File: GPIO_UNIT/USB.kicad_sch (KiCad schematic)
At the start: 11 parts, among them J701 USB_B_Mini, U701 CH340G, Y701 Crystal

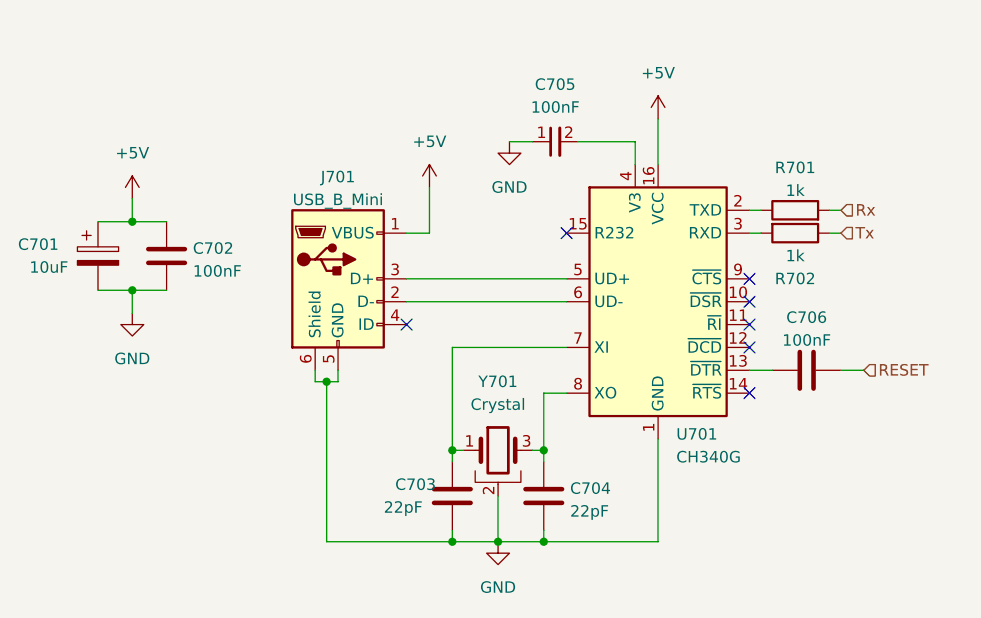
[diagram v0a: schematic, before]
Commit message: Digital pins are now able to use the analog pinnumbering as well. Pin can be set to an analog or digital pin number by simply pressing a or d respectively when editting the pinnumbers. Take note that one can fill in invalid analog pinnumbers. Also due to me support the arduino mega, I should remove pin number limit all togather.
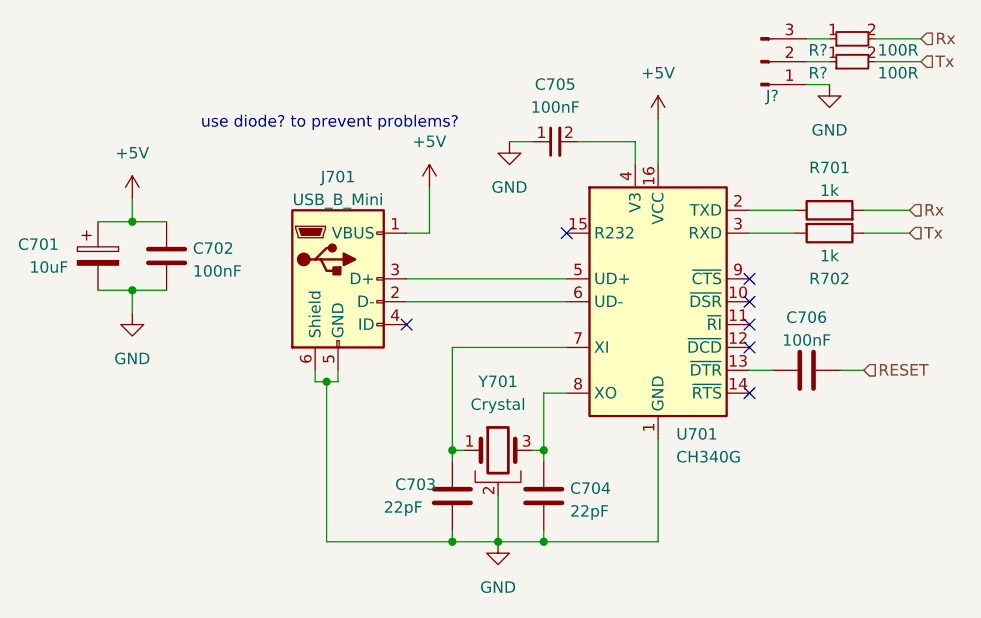
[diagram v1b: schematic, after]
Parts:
- added J?: Conn_01x03_Pin, symbol Connector:Conn_01x03_Pin
- added R? (x2): 100R, custom_kicad_lib_sk:R_0603_smalltext, symbol resistors_0603:R_100R_0603
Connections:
- net GND: now also J?.1 (Pin_1)
- net Rx: now also R?.2
- net Tx: now also R?.2
- new net: J?.3 (Pin_3), R?.1
- new net: J?.2 (Pin_2), R?.1
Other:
- note added: "use diode? to prevent problems?"
- moved on the sheet: R701, R702
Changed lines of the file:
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@@
     (stroke (width 0) (type default))
   )
-  (wire (pts (xy 134.62 83.82) (xy 133.35 83.82))
+  (wire (pts (xy 138.43 83.82) (xy 133.35 83.82))
     (stroke (width 0) (type default))
   )
@@
     (stroke (width 0) (type default))
   )
+  (wire (pts (xy 152.4 62.23) (xy 147.32 62.23))
+    (stroke (width 0) (type default))
+  )
   (wire (pts (xy 86.36 100.33) (xy 86.36 118.11))
     (stroke (width 0) (type default))
@@
     (stroke (width 0) (type default))
   )
-  (wire (pts (xy 143.51 83.82) (xy 142.24 83.82))
+  (wire (pts (xy 151.13 83.82) (xy 146.05 83.82))
     (stroke (width 0) (type default))
   )
@@
     (stroke (width 0) (type default))
   )
+  (wire (pts (xy 139.7 67.31) (xy 142.24 67.31))
+    (stroke (width 0) (type default))
+  )
   (wire (pts (xy 86.36 118.11) (xy 100.33 118.11))
     (stroke (width 0) (type default))
@@
     (stroke (width 0) (type default))
   )
+  (wire (pts (xy 139.7 64.77) (xy 142.24 64.77))
+    (stroke (width 0) (type default))
+  )
+  (wire (pts (xy 152.4 64.77) (xy 147.32 64.77))
+    (stroke (width 0) (type default))
+  )
   (wire (pts (xy 95.25 88.9) (xy 113.03 88.9))
     (stroke (width 0) (type default))
@@
     (stroke (width 0) (type default))
   )
+  (wire (pts (xy 139.7 62.23) (xy 142.24 62.23))
+    (stroke (width 0) (type default))
+  )
   (wire (pts (xy 113.03 96.52) (xy 100.33 96.52))
     (stroke (width 0) (type default))
@@
     (stroke (width 0) (type default))
   )
-  (wire (pts (xy 134.62 81.28) (xy 133.35 81.28))
+  (wire (pts (xy 138.43 81.28) (xy 133.35 81.28))
     (stroke (width 0) (type default))
   )
@@
     (stroke (width 0) (type default))
   )
-  (wire (pts (xy 143.51 81.28) (xy 142.24 81.28))
+  (wire (pts (xy 151.13 81.28) (xy 146.05 81.28))
     (stroke (width 0) (type default))
   )
@@
     (stroke (width 0) (type default))
   )
-  (hierarchical_label "Rx" (shape input) (at 143.51 81.28 0) (fields_autoplaced)
+  (text "use diode? to prevent problems?" (at 72.39 72.39 0)
+    (effects (font (size 1.27 1.27)) (justify left bottom))
+  )
+  (hierarchical_label "Tx" (shape input) (at 152.4 64.77 0) (fields_autoplaced)
     (effects (font (size 1.27 1.27)) (justify left))
   )
-  (hierarchical_label "Tx" (shape input) (at 143.51 83.82 0) (fields_autoplaced)
+  (hierarchical_label "Rx" (shape input) (at 152.4 62.23 0) (fields_autoplaced)
+    (effects (font (size 1.27 1.27)) (justify left))
+  )
+  (hierarchical_label "Rx" (shape input) (at 151.13 81.28 0) (fields_autoplaced)
+    (effects (font (size 1.27 1.27)) (justify left))
+  )
+  (hierarchical_label "Tx" (shape input) (at 151.13 83.82 0) (fields_autoplaced)
     (effects (font (size 1.27 1.27)) (justify left))
   )
@@
     )
   )
+  (symbol (lib_id "resistors_0603:R_100R_0603") (at 144.78 62.23 90) (unit 1)
+    (in_bom yes) (on_board yes) (dnp no)
+    (property "Reference" "R?" (at 140.97 63.5 90)
+      (effects (font (size 1.27 1.27)))
+    )
+    (property "Value" "100R" (at 149.86 63.5 90)
+      (effects (font (size 1.27 1.27)))
+    )
+    (property "Footprint" "custom_kicad_lib_sk:R_0603_smalltext" (at 142.24 59.69 0)
+      (effects (font (size 1.27 1.27)) hide)
+    )
+    (property "Datasheet" "" (at 144.78 64.77 0)
+      (effects (font (size 1.27 1.27)) hide)
+    )
+    (property "JLCPCB Part#" "C22775" (at 144.78 62.23 0)
+      (effects (font (size 1.27 1.27)) hide)
+    )
+    (pin "1")
+    (pin "2")
+    (instances
+      (project "GPIO_UNIT"
+        (path "/4337ba29-1ab5-4e01-8f76-ba2df9f917ea/a906ae47-0b9b-4d87-b0df-13938bf2addd"
+          (reference "R?") (unit 1)
+        )
+      )
+    )
+  )
   (symbol (lib_id "power:GND") (at 105.41 118.11 0) (unit 1)
     (in_bom yes) (on_board yes) (dnp no) (fields_autoplaced)
@@
     )
   )
-  (symbol (lib_id "Device:R") (at 138.43 83.82 270) (unit 1)
+  (symbol (lib_id "Device:R") (at 142.24 83.82 270) (unit 1)
     (in_bom yes) (on_board yes) (dnp no)
-    (property "Reference" "R702" (at 138.43 88.9 90)
-      (effects (font (size 1.27 1.27)))
-    )
-    (property "Value" "1k" (at 138.43 86.36 90)
-      (effects (font (size 1.27 1.27)))
-    )
-    (property "Footprint" "Resistor_SMD:R_0603_1608Metric" (at 138.43 82.042 90)
-      (effects (font (size 1.27 1.27)) hide)
-    )
-    (property "Datasheet" "~" (at 138.43 83.82 0)
-      (effects (font (size 1.27 1.27)) hide)
-    )
-    (property "JLCPCB Part#" "C21190" (at 138.43 83.82 90)
+    (property "Reference" "R702" (at 142.24 88.9 90)
+      (effects (font (size 1.27 1.27)))
+    )
+    (property "Value" "1k" (at 142.24 86.36 90)
+      (effects (font (size 1.27 1.27)))
+    )
+    (property "Footprint" "Resistor_SMD:R_0603_1608Metric" (at 142.24 82.042 90)
+      (effects (font (size 1.27 1.27)) hide)
+    )
+    (property "Datasheet" "~" (at 142.24 83.82 0)
+      (effects (font (size 1.27 1.27)) hide)
+    )
+    (property "JLCPCB Part#" "C21190" (at 142.24 83.82 90)
       (effects (font (size 1.27 1.27)) hide)
     )
@@
         (path "/fffcb7a4-8d9e-4797-952f-70897aee5417"
           (reference "R702") (unit 1)
+        )
+      )
+    )
+  )
+  (symbol (lib_id "resistors_0603:R_100R_0603") (at 144.78 64.77 90) (unit 1)
+    (in_bom yes) (on_board yes) (dnp no)
+    (property "Reference" "R?" (at 140.97 66.04 90)
+      (effects (font (size 1.27 1.27)))
+    )
+    (property "Value" "100R" (at 149.86 66.04 90)
+      (effects (font (size 1.27 1.27)))
+    )
+    (property "Footprint" "custom_kicad_lib_sk:R_0603_smalltext" (at 142.24 62.23 0)
+      (effects (font (size 1.27 1.27)) hide)
+    )
+    (property "Datasheet" "" (at 144.78 67.31 0)
+      (effects (font (size 1.27 1.27)) hide)
+    )
+    (property "JLCPCB Part#" "C22775" (at 144.78 64.77 0)
+      (effects (font (size 1.27 1.27)) hide)
+    )
+    (pin "1")
+    (pin "2")
+    (instances
+      (project "GPIO_UNIT"
+        (path "/4337ba29-1ab5-4e01-8f76-ba2df9f917ea/a906ae47-0b9b-4d87-b0df-13938bf2addd"
+          (reference "R?") (unit 1)
         )
       )
@@
     )
   )
-  (symbol (lib_id "Device:R") (at 138.43 81.28 90) (unit 1)
-    (in_bom yes) (on_board yes) (dnp no) (fields_autoplaced)
-    (property "Reference" "R701" (at 138.43 76.5642 90)
-      (effects (font (size 1.27 1.27)))
-    )
-    (property "Value" "1k" (at 138.43 79.1011 90)
-      (effects (font (size 1.27 1.27)))
-    )
-    (property "Footprint" "Resistor_SMD:R_0603_1608Metric" (at 138.43 83.058 90)
-      (effects (font (size 1.27 1.27)) hide)
-    )
-    (property "Datasheet" "~" (at 138.43 81.28 0)
-      (effects (font (size 1.27 1.27)) hide)
-    )
-    (property "JLCPCB Part#" "C21190" (at 138.43 81.28 90)
+  (symbol (lib_id "Connector:Conn_01x03_Pin") (at 134.62 64.77 0) (mirror x) (unit 1)
+    (in_bom yes) (on_board yes) (dnp no)
+    (property "Reference" "J?" (at 135.89 68.58 0)
+      (effects (font (size 1.27 1.27)))
+    )
+    (property "Value" "Conn_01x03_Pin" (at 135.255 69.85 0)
+      (effects (font (size 1.27 1.27)) hide)
+    )
+    (property "Footprint" "" (at 134.62 64.77 0)
+      (effects (font (size 1.27 1.27)) hide)
+    )
+    (property "Datasheet" "~" (at 134.62 64.77 0)
+      (effects (font (size 1.27 1.27)) hide)
+    )
+    (pin "3")
+    (pin "1")
+    (pin "2")
+    (instances
+      (project "GPIO_UNIT"
+        (path "/4337ba29-1ab5-4e01-8f76-ba2df9f917ea/a906ae47-0b9b-4d87-b0df-13938bf2addd"
+          (reference "J?") (unit 1)
+        )
+      )
+    )
+  )
+  (symbol (lib_id "Device:R") (at 142.24 81.28 90) (unit 1)
+    (in_bom yes) (on_board yes) (dnp no) (fields_autoplaced)
+    (property "Reference" "R701" (at 142.24 76.5642 90)
+      (effects (font (size 1.27 1.27)))
+    )
+    (property "Value" "1k" (at 142.24 79.1011 90)
+      (effects (font (size 1.27 1.27)))
+    )
+    (property "Footprint" "Resistor_SMD:R_0603_1608Metric" (at 142.24 83.058 90)
+      (effects (font (size 1.27 1.27)) hide)
+    )
+    (property "Datasheet" "~" (at 142.24 81.28 0)
+      (effects (font (size 1.27 1.27)) hide)
+    )
+    (property "JLCPCB Part#" "C21190" (at 142.24 81.28 90)
       (effects (font (size 1.27 1.27)) hide)
     )
@@
         )
       )
+    )
+  )
+  (symbol (lib_id "power:GND") (at 142.24 67.31 0) (unit 1)
+    (in_bom yes) (on_board yes) (dnp no) (fields_autoplaced)
+    (property "Reference" "#PWR0301" (at 142.24 73.66 0)
+      (effects (font (size 1.27 1.27)) hide)
+    )
+    (property "Value" "GND" (at 142.24 72.39 0)
+      (effects (font (size 1.27 1.27)))
+    )
+    (property "Footprint" "" (at 142.24 67.31 0)
+      (effects (font (size 1.27 1.27)) hide)
+    )
+    (property "Datasheet" "" (at 142.24 67.31 0)
+      (effects (font (size 1.27 1.27)) hide)
+    )
+    (pin "1")
+    (instances
+      (project "GPIO_UNIT"
+        (path "/4337ba29-1ab5-4e01-8f76-ba2df9f917ea/a906ae47-0b9b-4d87-b0df-13938bf2addd"
+          (reference "#PWR0301") (unit 1)
+        )
+      )
